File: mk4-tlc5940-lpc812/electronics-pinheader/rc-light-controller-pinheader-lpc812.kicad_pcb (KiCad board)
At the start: 2 copper layers, 44 x 23 mm, 14 parts, among them J1 Conn_02x17_Odd_Even, J2 Conn_01x06, J3 Conn_01x06, T9 PMV30UN, U1 LPC812M101JDH20, U2 TLC5940PWP, U3 MCP1703A-3302_SOT23

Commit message: Tweak schematics, layout text and add BOM CSV files
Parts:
- J1: value Conn_02x17_Odd_Even -> Pinheader right-angle 2x17
- J2, J3: value Conn_01x06 -> Pinheader straight 1x06

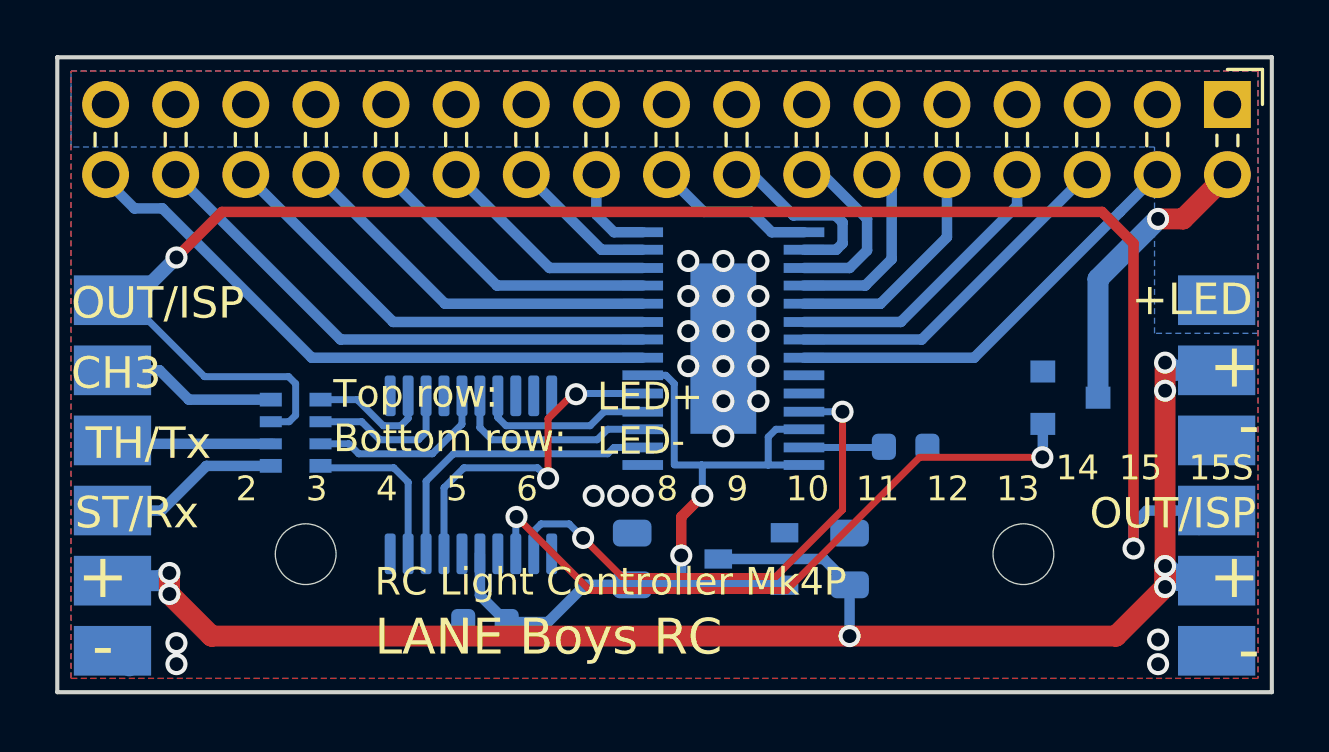
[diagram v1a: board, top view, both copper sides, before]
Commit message: Swap VIN and LED+, add version detection
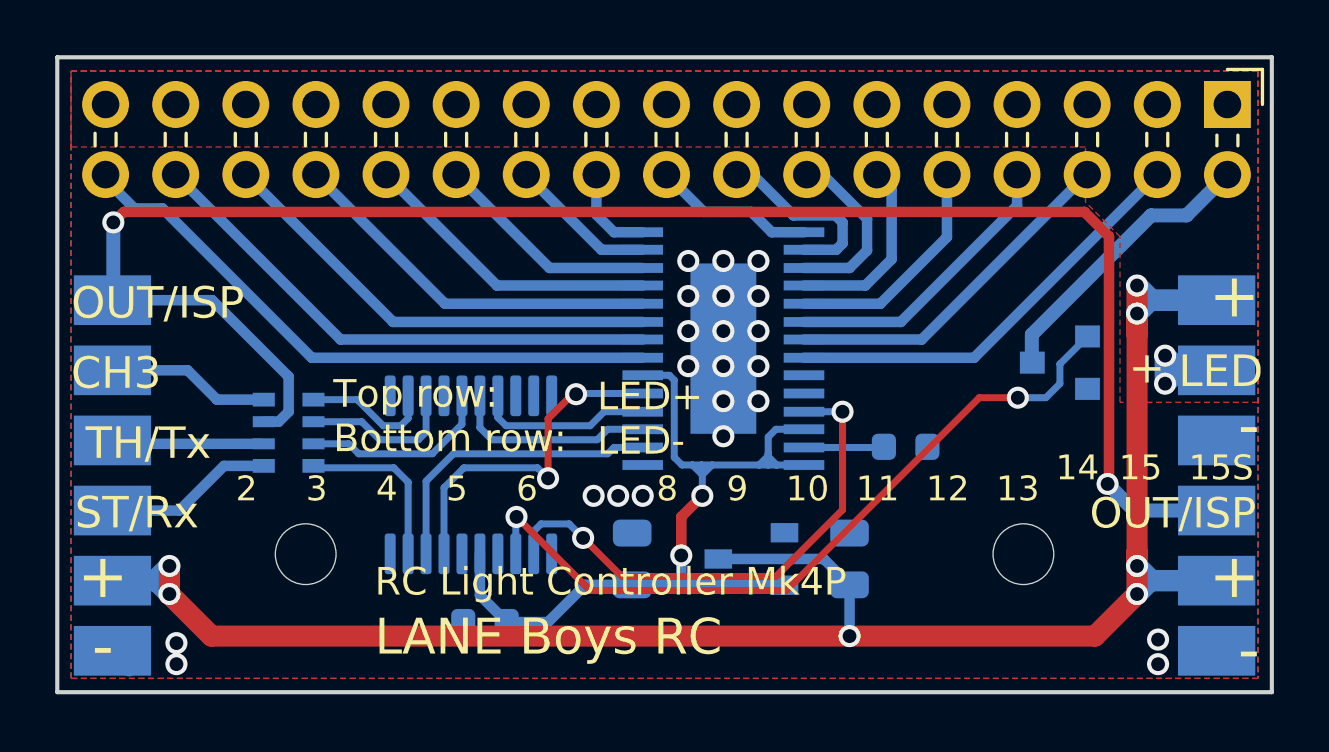
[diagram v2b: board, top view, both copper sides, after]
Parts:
- moved T9 1.33 mm to (171.3, 102.1), turned to 180 degrees
- moved RN1 0.25 mm to (143.4, 104.6)
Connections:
- J3 pad 5: /VIN -> /LED+
- J3 pad 6: /LED+ -> /VIN
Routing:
- net /VIN: track 60.3 -> 76.5 mm
- net /LED+: track 0.00 -> 5.17 mm, vias 0 -> 2
- net /OUT15S: track 24.7 -> 27.4 mm
- net +3V3: track 29.6 -> 31.5 mm
- net /OUT15S_OUT: track 10.6 -> 10.5 mm, vias 1 -> 0
- added copper zone on F.Cu, net /LED+
- removed copper zone on B.Cu, net /LED+
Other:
- board text added: "LED"
- board text removed: "+LED"

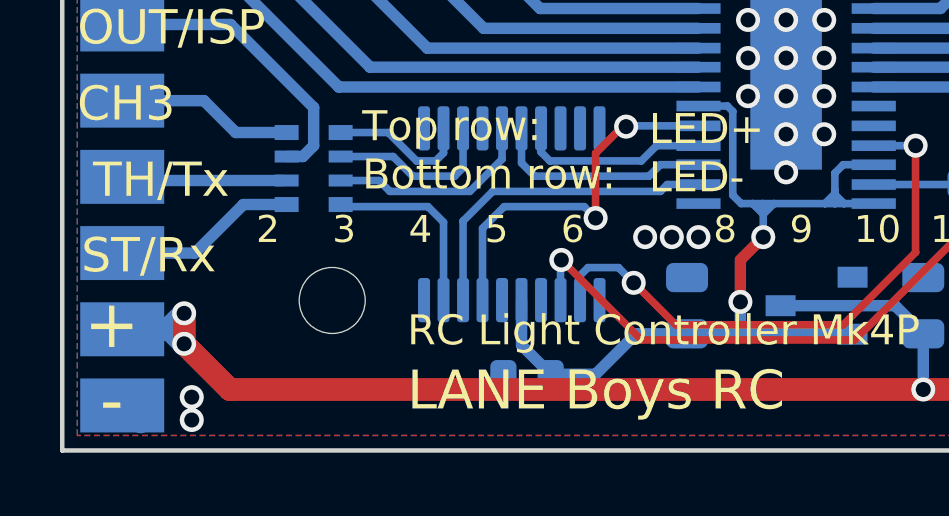
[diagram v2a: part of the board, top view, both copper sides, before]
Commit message: Add more dimensions; Add supply voltage on silk screen
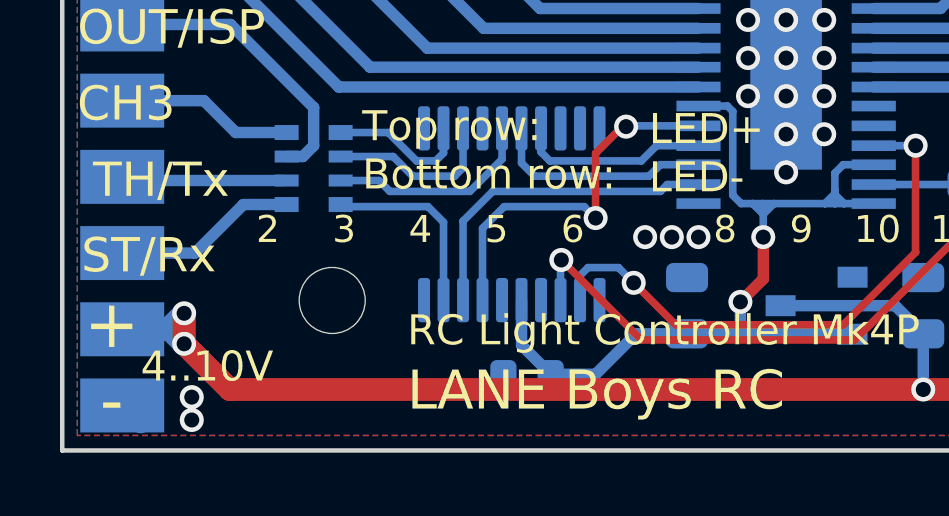
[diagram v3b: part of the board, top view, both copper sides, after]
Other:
- board text added: "4..10V"
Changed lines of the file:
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@@
   (general
     (thickness 1.6)
-    (drawings 41)
+    (drawings 46)
     (tracks 257)
     (zones 0)
@@
     (33 F.Adhes user hide)
     (34 B.Paste user)
-    (35 F.Paste user)
+    (35 F.Paste user hide)
     (36 B.SilkS user)
     (37 F.SilkS user)
     (38 B.Mask user)
     (39 F.Mask user)
-    (40 Dwgs.User user)
-    (41 Cmts.User user hide)
+    (40 Dwgs.User user hide)
+    (41 Cmts.User user)
     (42 Eco1.User user hide)
     (43 Eco2.User user hide)
     (44 Edge.Cuts user)
-    (45 Margin user)
+    (45 Margin user hide)
     (46 B.CrtYd user)
     (47 F.CrtYd user)
-    (48 B.Fab user hide)
-    (49 F.Fab user hide)
+    (48 B.Fab user)
+    (49 F.Fab user)
   )
   (setup
@@
       (effects (font (size 1 1) (thickness 0.15)))
     )
-    (fp_text value MountingHole (at 0 2.9) (layer F.Fab)
+    (fp_text value MountingHole (at 0 2.9) (layer F.Fab) hide
       (effects (font (size 1 1) (thickness 0.15)))
     )
@@
       (effects (font (size 1 1) (thickness 0.15)))
     )
-    (fp_text value MountingHole (at 0 2.9) (layer F.Fab)
+    (fp_text value MountingHole (at 0 2.9) (layer F.Fab) hide
       (effects (font (size 1 1) (thickness 0.15)))
     )
@@
     )
   )
+  (gr_text 4..10V (at 139.826 111.206) (layer F.SilkS)
+    (effects (font (size 1 1) (thickness 0.2)))
+  )
+  (dimension 9 (width 0.15) (layer Cmts.User)
+    (gr_text "9.000 mm" (at 174.5 117.3) (layer Cmts.User)
+      (effects (font (size 1 1) (thickness 0.15)))
+    )
+    (feature1 (pts (xy 179 109) (xy 179 116.586421)))
+    (feature2 (pts (xy 170 109) (xy 170 116.586421)))
+    (crossbar (pts (xy 170 116) (xy 179 116)))
+    (arrow1a (pts (xy 179 116) (xy 177.873496 116.586421)))
+    (arrow1b (pts (xy 179 116) (xy 177.873496 115.413579)))
+    (arrow2a (pts (xy 170 116) (xy 171.126504 116.586421)))
+    (arrow2b (pts (xy 170 116) (xy 171.126504 115.413579)))
+  )
+  (dimension 5 (width 0.15) (layer Cmts.User)
+    (gr_text "5.000 mm" (at 131.7 111.5 90) (layer Cmts.User)
+      (effects (font (size 1 1) (thickness 0.15)))
+    )
+    (feature1 (pts (xy 144 109) (xy 132.413579 109)))
+    (feature2 (pts (xy 144 114) (xy 132.413579 114)))
+    (crossbar (pts (xy 133 114) (xy 133 109)))
+    (arrow1a (pts (xy 133 109) (xy 133.586421 110.126504)))
+    (arrow1b (pts (xy 133 109) (xy 132.413579 110.126504)))
+    (arrow2a (pts (xy 133 114) (xy 133.586421 112.873496)))
+    (arrow2b (pts (xy 133 114) (xy 132.413579 112.873496)))
+  )
+  (dimension 35 (width 0.15) (layer Cmts.User)
+    (gr_text "35.000 mm" (at 152.5 120.3) (layer Cmts.User)
+      (effects (font (size 1 1) (thickness 0.15)))
+    )
+    (feature1 (pts (xy 170 109) (xy 170 119.586421)))
+    (feature2 (pts (xy 135 109) (xy 135 119.586421)))
+    (crossbar (pts (xy 135 119) (xy 170 119)))
+    (arrow1a (pts (xy 170 119) (xy 168.873496 119.586421)))
+    (arrow1b (pts (xy 170 119) (xy 168.873496 118.413579)))
+    (arrow2a (pts (xy 135 119) (xy 136.126504 119.586421)))
+    (arrow2b (pts (xy 135 119) (xy 136.126504 118.413579)))
+  )
+  (dimension 9 (width 0.15) (layer Cmts.User)
+    (gr_text "9.000 mm" (at 139.5 117.3) (layer Cmts.User)
+      (effects (font (size 1 1) (thickness 0.15)))
+    )
+    (feature1 (pts (xy 144 109) (xy 144 116.586421)))
+    (feature2 (pts (xy 135 109) (xy 135 116.586421)))
+    (crossbar (pts (xy 135 116) (xy 144 116)))
+    (arrow1a (pts (xy 144 116) (xy 142.873496 116.586421)))
+    (arrow1b (pts (xy 144 116) (xy 142.873496 115.413579)))
+    (arrow2a (pts (xy 135 116) (xy 136.126504 116.586421)))
+    (arrow2b (pts (xy 135 116) (xy 136.126504 115.413579)))
+  )
   (gr_text + (at 175.132 102.2525) (layer F.SilkS)
     (effects (font (size 1.143 1.143) (thickness 0.28575)) (justify right))
@@
   )
   (dimension 15 (width 0.15) (layer Cmts.User)
-    (gr_text "15.000 mm" (at 170.3 106.5 90) (layer Cmts.User)
+    (gr_text "15.000 mm" (at 128.7 106.5 90) (layer Cmts.User)
       (effects (font (size 1 1) (thickness 0.15)))
     )
-    (feature1 (pts (xy 169 99) (xy 169.586421 99)))
-    (feature2 (pts (xy 169 114) (xy 169.586421 114)))
-    (crossbar (pts (xy 169 114) (xy 169 99)))
-    (arrow1a (pts (xy 169 99) (xy 169.586421 100.126504)))
-    (arrow1b (pts (xy 169 99) (xy 168.413579 100.126504)))
-    (arrow2a (pts (xy 169 114) (xy 169.586421 112.873496)))
-    (arrow2b (pts (xy 169 114) (xy 168.413579 112.873496)))
+    (feature1 (pts (xy 135 99) (xy 129.413579 99)))
+    (feature2 (pts (xy 135 114) (xy 129.413579 114)))
+    (crossbar (pts (xy 130 114) (xy 130 99)))
+    (arrow1a (pts (xy 130 99) (xy 130.586421 100.126504)))
+    (arrow1b (pts (xy 130 99) (xy 129.413579 100.126504)))
+    (arrow2a (pts (xy 130 114) (xy 130.586421 112.873496)))
+    (arrow2b (pts (xy 130 114) (xy 129.413579 112.873496)))
   )
   (gr_text JLCJLCJLCJLC (at 174.37 112.776) (layer B.SilkS)
@@
   )
   (dimension 44 (width 0.3) (layer Cmts.User)
-    (gr_text "44.000 mm" (at 157 118.1) (layer Cmts.User)
+    (gr_text "44.000 mm" (at 157 124.1) (layer Cmts.User)
       (effects (font (size 1.5 1.5) (thickness 0.3)))
     )
-    (feature1 (pts (xy 179 114) (xy 179 116.586421)))
-    (feature2 (pts (xy 135 114) (xy 135 116.586421)))
-    (crossbar (pts (xy 135 116) (xy 179 116)))
-    (arrow1a (pts (xy 179 116) (xy 177.873496 116.586421)))
-    (arrow1b (pts (xy 179 116) (xy 177.873496 115.413579)))
-    (arrow2a (pts (xy 135 116) (xy 136.126504 116.586421)))
-    (arrow2b (pts (xy 135 116) (xy 136.126504 115.413579)))
+    (feature1 (pts (xy 179 114) (xy 179 122.586421)))
+    (feature2 (pts (xy 135 114) (xy 135 122.586421)))
+    (crossbar (pts (xy 135 122) (xy 179 122)))
+    (arrow1a (pts (xy 179 122) (xy 177.873496 122.586421)))
+    (arrow1b (pts (xy 179 122) (xy 177.873496 121.413579)))
+    (arrow2a (pts (xy 135 122) (xy 136.126504 122.586421)))
+    (arrow2b (pts (xy 135 122) (xy 136.126504 121.413579)))
   )
   (gr_text Rev1 (at 146.073929 112.349) (layer B.SilkS)
@@
   (segment (start 158.368 105.7958) (end 158.3426 105.7704) (width 0.254) (layer Bottom) (net 1))
   (segment (start 157.606 109.047) (end 157.606 110.063) (width 0.381) (layer Bottom) (net 1))
-  (segment (start 157.606 107.65) (end 158.368 106.888) (width 0.381) (layer Top) (net 1))
   (via (at 157.606 109.047) (size 0.8) (drill 0.5) (layers Top Bottom) (net 1))
-  (segment (start 157.606 109.047) (end 157.606 107.65) (width 0.381) (layer Top) (net 1))
   (segment (start 158.368 106.126) (end 158.7236 105.7704) (width 0.254) (layer Bottom) (net 1))
   (segment (start 158.7236 105.7704) (end 158.3426 105.7704) (width 0.254) (layer Bottom) (net 1))
@@
   (segment (start 158.0124 105.7704) (end 157.6314 105.7704) (width 0.254) (layer Bottom) (net 1))
   (segment (start 157.6314 105.7704) (end 157.352 105.491) (width 0.254) (layer Bottom) (net 1))
+  (segment (start 158.368 108.285) (end 158.368 106.888) (width 0.381) (layer Top) (net 1))
+  (segment (start 157.606 109.047) (end 158.368 108.285) (width 0.381) (layer Top) (net 1))
   (via (at 159.13 103.459) (size 0.8) (drill 0.5) (layers Top Bottom) (net 2) (status 30))
   (via (at 159.13 102.189) (size 0.8) (drill 0.5) (layers Top Bottom) (net 2) (status 30))
@@
   )
   (zone (net 2) (net_name GND) (layer Top) (hatch edge 0.508)
-    (connect_pads (clearance 0.3048))
+    (connect_pads (clearance 0.254))
     (min_thickness 0.254)
     (fill yes (arc_segments 32) (thermal_gap 0.3556) (thermal_bridge_width 0.3556))
